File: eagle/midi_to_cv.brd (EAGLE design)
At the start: 100.3 x 80 mm, 26 parts, among them U1 ATMEGA328P_PDIP

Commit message: noise and accent and raw gates
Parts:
- added C10: 47n, rcl:C025-040X050
- added C11: 2n7, rcl:C025-040X050
- added C12: 2n2, rcl:C025-040X050
- added C13: 1u/50v, rcl:B45181A
- added C8: 470pF, rcl:C025-040X050
- added C9: 18p, rcl:C025-040X050
- added D1, D3: (no value), SparkFun-DiscreteSemi:DIODE-1N4148
- added JP1: (no value), adafruit:2X04
- added OUTPUT: 22-23-2021, con-molex:22-23-2021
- added Q10, Q11, Q12, Q13, Q14, Q15, Q16, Q2, Q3, Q4, Q5, Q7, Q8, Q9: 2N3904, 808_lt:TO92
- added Q6: 2SK30, 808:TO92
- added R10: 1M5, rcl:0207/10
- added R11, R18, R20, R23, R25, R27, R29, R3, R31, R33, R35, R37: 15k, rcl:0207/10
- added R12: 47k, rcl:0207/10
- added R13: 100k, rcl:0207/10
- added R14: 2M2, rcl:0207/10
- added R16, R19, R21, R24, R26, R28, R30, R32, R34, R36, R38, R8, R9: 68k, rcl:0207/10
- added R17: 100k, pot:3RP/1610N
- added R7: 1M, rcl:0207/10
- added X1, X3: (no value), con-molex:22-23-2061
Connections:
- new net GND1: JP1.2, JP1.4, JP1.6, JP1.8, Q4.1, R10.2
- new net N$13: Q4.2, R10.1, R9.2
- new net N$14: Q7.1, R18.2
- new net N$15: C9.1, Q5.1, R11.2
- new net N$16: Q5.2, R12.2
- new net N$21: C9.2, D1.A, R13.1
- new net N$22: C10.1, D1.C, D3.C, R14.1
- new net N$23: D3.A, Q6.2
- new net N$24: C12.1, R16.1, R17.2, X1.1, X1.2, X1.3, X1.4, X1.5, X1.6, X3.1, X3.2, X3.3, X3.4, X3.5, X3.6
- new net N$25: Q7.2, R19.2
- new net N$26: C13.-, OUTPUT.2
- new net N$27: Q8.1, R20.2
- new net N$28: Q8.2, R21.2
- new net N$29: C11.1, C12.2, Q6.1, R17.3
- new net N$3: Q2.1, R3.2
- new net N$30: Q9.1, R23.2
- new net N$31: Q9.2, R24.2
- new net N$32: C11.2, C13.+, Q6.3, R16.2
- new net N$33: Q10.1, R25.2
- new net N$34: Q10.2, R26.2
- new net N$35: R21.1, U1.23
- new net N$36: Q11.1, R27.2
- new net N$37: Q11.2, R28.2
- new net N$38: Q12.1, R29.2
- new net N$39: Q12.2, R30.2
- new net N$40: Q13.1, R31.2
- new net N$41: Q13.2, R32.2
- new net N$42: Q14.1, R33.2
- new net N$43: Q14.2, R34.2
- new net N$44: Q15.1, R35.2
- new net N$45: Q15.2, R36.2
- new net N$46: Q16.1, R37.2
- new net N$47: Q16.2, R38.2
- new net N$48: R30.1, U1.24
- new net N$49: R36.1, U1.25
- new net N$50: R8.1, U1.26
- new net N$51: R19.1, U1.28
- new net N$52: R28.1, U1.27
- new net N$53: R34.1, U1.4
- new net N$54: R26.1, U1.5
- new net N$55: R24.1, U1.6
- new net N$56: R32.1, U1.11
- new net N$57: R38.1, U1.12
- new net N$6: C8.1, Q3.3, R7.2
- new net N$7: Q2.2, R8.2
- new net N$8: C8.2, R9.1
- net +12V: now also R11.1, R18.1, R20.1, R23.1, R25.1, R27.1, R29.1, R3.1, R31.1, R33.1, R35.1, R37.1, R7.1
- net GND: now also C10.2, JP1.1, JP1.3, JP1.5, JP1.7, OUTPUT.1, Q10.3, Q11.3, Q12.3, Q13.3, Q14.3, Q15.3, Q16.3, Q2.3, Q3.2, Q4.3, Q5.3, Q7.3, Q8.3, Q9.3, R13.2

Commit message: connectors for each voice
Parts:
- removed JP1: (no value), adafruit:2X04
- removed LED: 22-23-2021, con-molex:22-23-2021
- removed MIDI_OUT_THRU1: 22-23-2031, con-molex:22-23-2031
- removed Q10, Q11, Q12, Q13, Q14, Q15, Q16, Q2, Q7, Q8, Q9: 2N3904, 808_lt:TO92
- removed R18, R20, R23, R25, R27, R29, R3, R31, R33, R35, R37: 15k, rcl:0207/10
- removed R19, R21, R24, R26, R28, R30, R32, R34, R36, R38, R8: 68k, rcl:0207/10
- removed R2: 220, rcl:0207/10
- removed R4: 4.7k, rcl:0207/10
- removed X1, X3: (no value), con-molex:22-23-2061
- added BD, HB, LB, LC: 22-23-2041, con-molex:22-23-2041
- added CB, C_RS, MB, SD: 22-23-2051, con-molex:22-23-2051
- added CY, GU, HH, M: (no value), con-molex:22-23-2061
- added TB: 22-23-2071, con-molex:22-23-2071
- R1, R10, R11, R13, R14, R16, R22, R6, R7, R9: device rcl:0207/10 -> rcl:0204/7
- R12: device rcl:0207/10 -> rcl:0207/12
- moved C13 180.3 mm to (21.6, 20.3), turned to 270 degrees
- moved OUTPUT 169.2 mm to (24.1, 10.2), turned to 180 degrees
- moved R16 151.8 mm to (20.3, 10.2), turned to 90 degrees
- moved C12 146.3 mm to (11.4, 12.7)
- moved C11 142.9 mm to (16.5, 17.8)
- moved R17 133.6 mm to (10.2, 3.81)
- moved Q6 125.4 mm to (17.8, 24.1), turned to 90 degrees
- moved C8 113.7 mm to (74.9, 53.3)
- moved D3 113.1 mm to (8.89, 17.8), turned to 180 degrees
- moved R14 111.8 mm to (2.54, 20.3), turned to 90 degrees
- moved C10 111.8 mm to (3.81, 27.9), turned to 180 degrees
- moved R10 109.2 mm to (66.0, 44.5), turned to 270 degrees
- moved Q4 107.1 mm to (62.2, 47.0), turned to 270 degrees
- moved R13 106.7 mm to (6.35, 31.8), turned to 180 degrees
- moved R12 105.6 mm to (24.1, 41.9), turned to 270 degrees
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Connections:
- removed net GND1: JP1.2, JP1.4, JP1.6, JP1.8, Q4.1, R10.2
- removed net N$10: R4.2, U1.19
- removed net N$11: LED.2, R4.1
- removed net N$12: MIDI_OUT_THRU1.2, U1.3
- removed net N$27: Q8.1, R20.2
- removed net N$28: Q8.2, R21.2
- removed net N$30: Q9.1, R23.2
- removed net N$31: Q9.2, R24.2
- removed net N$33: Q10.1, R25.2
- removed net N$34: Q10.2, R26.2
- removed net N$35: R21.1, U1.23
- removed net N$36: Q11.1, R27.2
- removed net N$37: Q11.2, R28.2
- removed net N$38: Q12.1, R29.2
- removed net N$39: Q12.2, R30.2
- removed net N$40: Q13.1, R31.2
- removed net N$41: Q13.2, R32.2
- removed net N$42: Q14.1, R33.2
- removed net N$43: Q14.2, R34.2
- removed net N$44: Q15.1, R35.2
- removed net N$45: Q15.2, R36.2
- removed net N$46: Q16.1, R37.2
- removed net N$47: Q16.2, R38.2
- removed net N$48: R30.1, U1.24
- removed net N$49: R36.1, U1.25
- removed net N$50: R8.1, U1.26
- removed net N$51: R19.1, U1.28
- removed net N$52: R28.1, U1.27
- removed net N$53: R34.1, U1.4
- removed net N$54: R26.1, U1.5
- removed net N$55: R24.1, U1.6
- removed net N$56: R32.1, U1.11
- removed net N$57: R38.1, U1.12
- removed net N$9: MIDI_OUT_THRU1.1, R2.2
- new net ACCENT: R12.1, U1.5
- new net CB_TRIG: CB.1, U1.28
- new net CY_KILL: CY.2, HH.2, M.2, U1.14
- new net CY_TRIG: CY.1, U1.16
- new net C_TRIG: C_RS.2, U1.18
- new net GU_LONG: GU.1, U1.3
- new net GU_SHORT: GU.2, U1.4
- new net HH_TRIG: HH.1, U1.15
- new net M_TRIG: M.1, U1.13
- new net NOISE: CY.3, GU.3, HH.3, M.3, Q4.1, R10.2, SD.2, TB.4
- new net RETURN: BD.4, C12.1, CB.5, CY.6, C_RS.5, GU.6, HB.4, HH.6, LB.4, LC.4, M.6, MB.5, R16.1, R17.2, SD.5, TB.7
- new net RS_TRIG: C_RS.1, U1.17
- new net SD_TRIG: SD.1, U1.19
- new net TB_KILL: TB.3, U1.12
- new net TB_LONG: TB.1, U1.6
- new net TB_SHORT: TB.2, U1.11
- net +12V: now also BD.2, CB.3, CY.4, C_RS.3, GU.4, HB.2, HH.4, LB.2, LC.2, M.4, MB.3, SD.3, TB.5; no longer R18.1, R20.1, R23.1, R25.1, R27.1, R29.1, R3.1, R31.1, R33.1, R35.1, R37.1
- net +5V: now also CB.2, MB.2; no longer R2.1
- net GND: now also BD.3, CB.4, CY.5, C_RS.4, GU.5, HB.3, HH.5, LB.3, LC.3, M.5, MB.4, R14.2, SD.4, TB.6; no longer JP1.1, JP1.3, JP1.5, JP1.7, LED.1, MIDI_OUT_THRU1.3, Q10.3, Q11.3, Q12.3, Q13.3, Q14.3, Q15.3, Q16.3, Q2.3, Q7.3, Q8.3, Q9.3
- net N$14: now also HB.1, U1.25; no longer Q7.1, R18.2
- net N$24: now also MB.1, U1.27; no longer C12.1, R16.1, R17.2, X1.1, X1.2, X1.3, X1.4, X1.5, X1.6, X3.1, X3.2, X3.3, X3.4, X3.5, X3.6
- net N$25: now also LC.1, U1.26; no longer Q7.2, R19.2
- net N$3: now also BD.1, U1.23; no longer Q2.1, R3.2
- net N$7: now also LB.1, U1.24; no longer Q2.2, R8.2
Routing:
- net +5V: track 230.1 -> 0.00 mm, vias 6 -> 0
- net GND: track 177.2 -> 0.00 mm
- net +12V: track 158.0 -> 0.00 mm, vias 2 -> 0
- net N$17: track 22.8 -> 0.00 mm
- net N$62: track 17.8 -> 0.00 mm
- net N$20: track 17.7 -> 0.00 mm
- net N$12: track 16.9 -> 0.00 mm
- net N$2: track 16.8 -> 0.00 mm
- net N$10: track 16.7 -> 0.00 mm
- net N$5: track 15.6 -> 0.00 mm
- net N$4: track 13.3 -> 0.00 mm
- net N$18: track 13.0 -> 0.00 mm
- net N$60: track 12.4 -> 0.00 mm
- net N$19: track 10.6 -> 0.00 mm
- net N$1: track 6.57 -> 0.00 mm
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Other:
- board size 100.3 x 80 mm -> 100 x 80 mm

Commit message: 95pct auto
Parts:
- C9: device rcl:C025-040X050 -> rcl:C050-025X075
- moved R14 65.1 mm to (67.3, 14.0), turned to 270 degrees
- moved Q5 65.0 mm to (80.0, 29.2), turned to 90 degrees
- moved R17 63.5 mm to (73.7, 3.81)
- moved C10 62.5 mm to (64.8, 14.0), turned to 270 degrees
- moved C9 62.3 mm to (73.7, 30.5)
- moved D3 62.3 mm to (71.1, 20.3)
- moved C12 62.2 mm to (73.7, 11.4)
- moved R13 61.3 mm to (67.3, 25.4)
- moved R11 60.3 mm to (78.7, 38.1), turned to 270 degrees
- moved C13 59.8 mm to (81.3, 24.1)
- moved D1 59.7 mm to (67.3, 22.9), turned to 180 degrees
- moved Q6 59.7 mm to (77.5, 24.1)
- moved C11 57.2 mm to (73.7, 15.2), turned to 180 degrees
- moved OUTPUT 54.7 mm to (78.7, 14.0)
- moved R16 49.6 mm to (69.8, 12.7)
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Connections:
- removed net GU_LONG: GU.1, U1.3
- removed net GU_SHORT: GU.2, U1.4
- new net N$10: GU.2, U1.19
- new net N$9: GU.1, U1.18
- net ACCENT: now also U1.28; no longer U1.5
- net CB_TRIG: now also U1.5; no longer U1.28
- net CY_KILL: now also U1.13; no longer U1.14
- net C_TRIG: now also U1.24; no longer U1.18
- net M_TRIG: now also U1.14; no longer U1.13
- net N$3: now also U1.3; no longer U1.23
- net N$7: now also U1.4; no longer U1.24
- net RS_TRIG: now also U1.23; no longer U1.17
- net SD_TRIG: now also U1.17; no longer U1.19
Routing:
- net GND: track 0.00 -> 442.4 mm
- net RETURN: track 0.00 -> 227.4 mm
- net +12V: track 0.00 -> 174.4 mm
- net +5V: track 0.00 -> 80.8 mm
- net NOISE: track 0.00 -> 72.5 mm
- net CY_KILL: track 0.00 -> 47.1 mm
- net N$5: track 0.00 -> 29.7 mm
- net HH_TRIG: track 0.00 -> 22.8 mm
- net TB_KILL: track 0.00 -> 22.5 mm
- net N$17: track 0.00 -> 22.5 mm
- net N$29: track 0.00 -> 21.8 mm
- net TB_SHORT: track 0.00 -> 20.9 mm
- net N$32: track 0.00 -> 20.5 mm
- net N$7: track 0.00 -> 20.3 mm
- net N$4: track 0.00 -> 19.5 mm
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
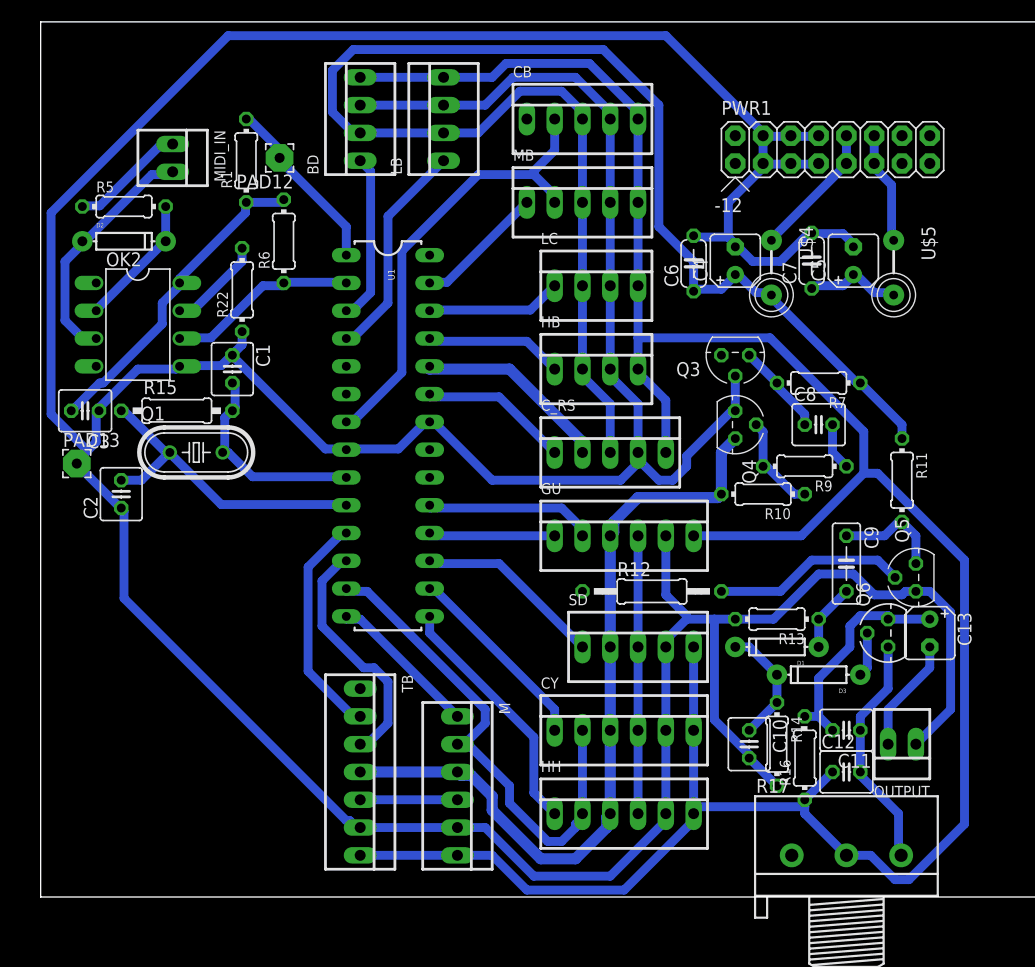
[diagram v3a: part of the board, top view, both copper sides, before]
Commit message: added midi led and thru
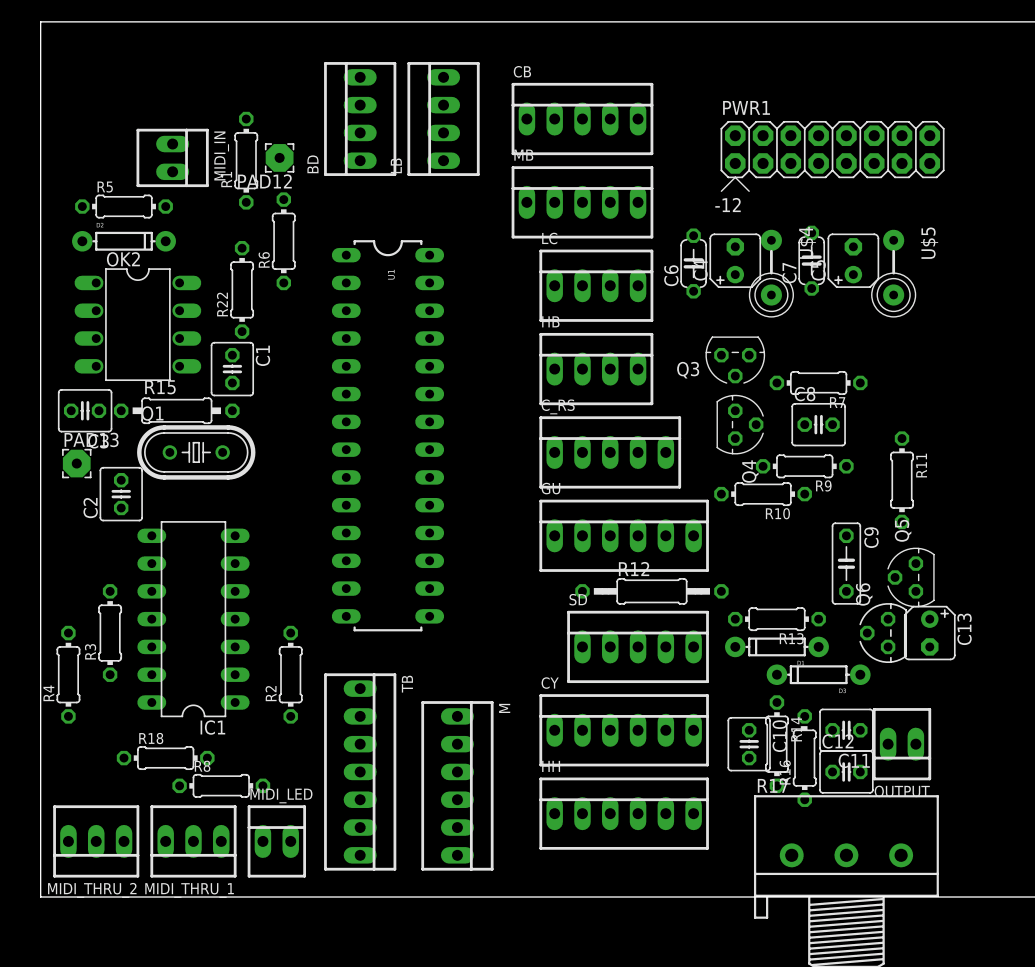
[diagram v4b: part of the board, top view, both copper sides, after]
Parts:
- added IC1: 4093N, 40xx:DIL14
- added MIDI_LED: 22-23-2021, con-molex:22-23-2021
- added MIDI_THRU_1, MIDI_THRU_2: 22-23-2031, con-molex:22-23-2031
- added R18, R3, R4, R8: 220, rcl:0204/7
- added R2: 330, rcl:0204/7
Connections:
- new net N$11: IC1.1, IC1.2, OK2.6, R6.1, U1.2
- new net N$12: IC1.4, R2.2
- new net N$27: IC1.10, R3.2
- new net N$28: IC1.11, R4.2
- new net N$30: IC1.12, IC1.13, IC1.3, IC1.5, IC1.6, IC1.8, IC1.9
- new net N$31: MIDI_LED.2, R2.1
- new net N$33: MIDI_THRU_1.3, R3.1
- new net N$34: MIDI_THRU_2.3, R4.1
- new net N$35: MIDI_THRU_2.1, R18.1
- net +5V: now also IC1.14, MIDI_LED.1, R18.2, R8.2
- net GND: now also IC1.7, MIDI_THRU_1.2, MIDI_THRU_2.2
- net N$20: now also MIDI_THRU_1.1, R8.1; no longer OK2.6, R6.1, U1.2
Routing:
- net GND: track 442.4 -> 0.00 mm
- net RETURN: track 227.4 -> 0.00 mm
- net +12V: track 174.4 -> 0.00 mm
- net +5V: track 80.8 -> 0.00 mm
- net NOISE: track 72.5 -> 0.00 mm
- net CY_KILL: track 47.1 -> 0.00 mm
- net N$5: track 29.7 -> 0.00 mm
- net HH_TRIG: track 22.8 -> 0.00 mm
- net TB_KILL: track 22.5 -> 0.00 mm
- net N$17: track 22.5 -> 0.00 mm
- net N$29: track 21.8 -> 0.00 mm
- net TB_SHORT: track 20.9 -> 0.00 mm
- net N$32: track 20.5 -> 0.00 mm
- net N$7: track 20.3 -> 0.00 mm
- net N$4: track 19.5 -> 0.00 mm
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
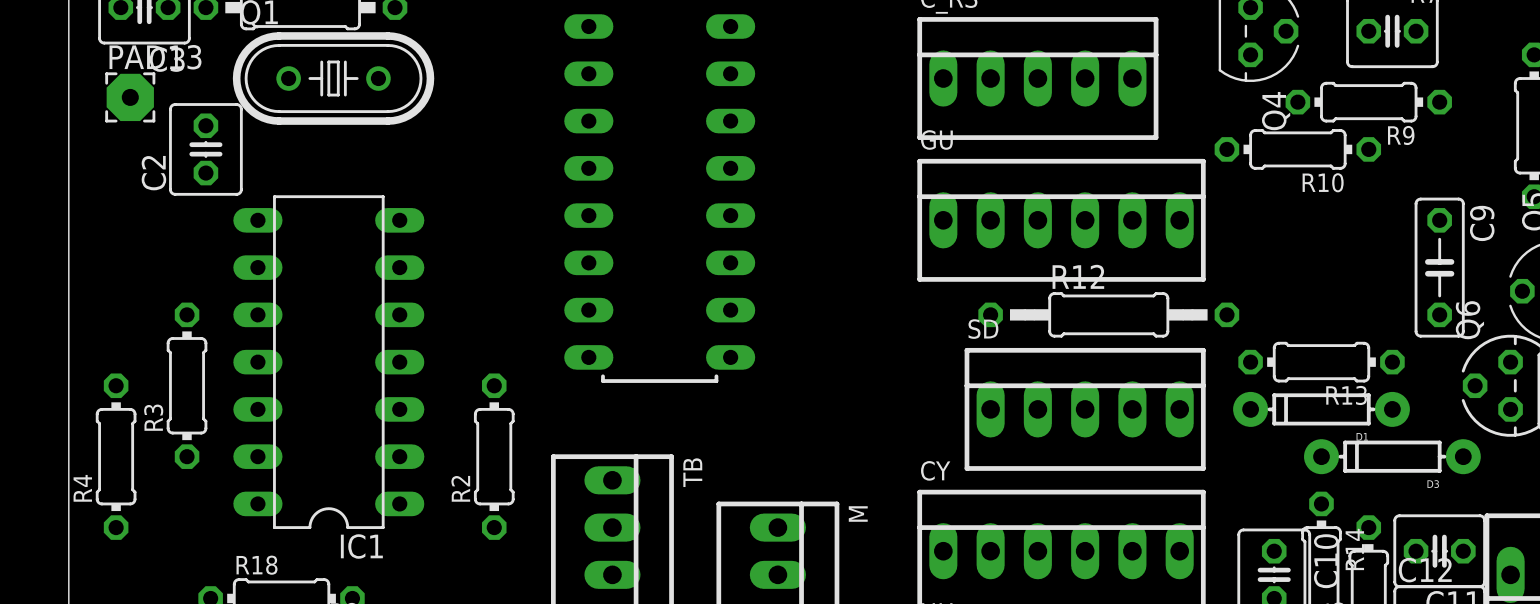
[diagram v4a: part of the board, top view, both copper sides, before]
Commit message: shifted accent pin closer to circuit
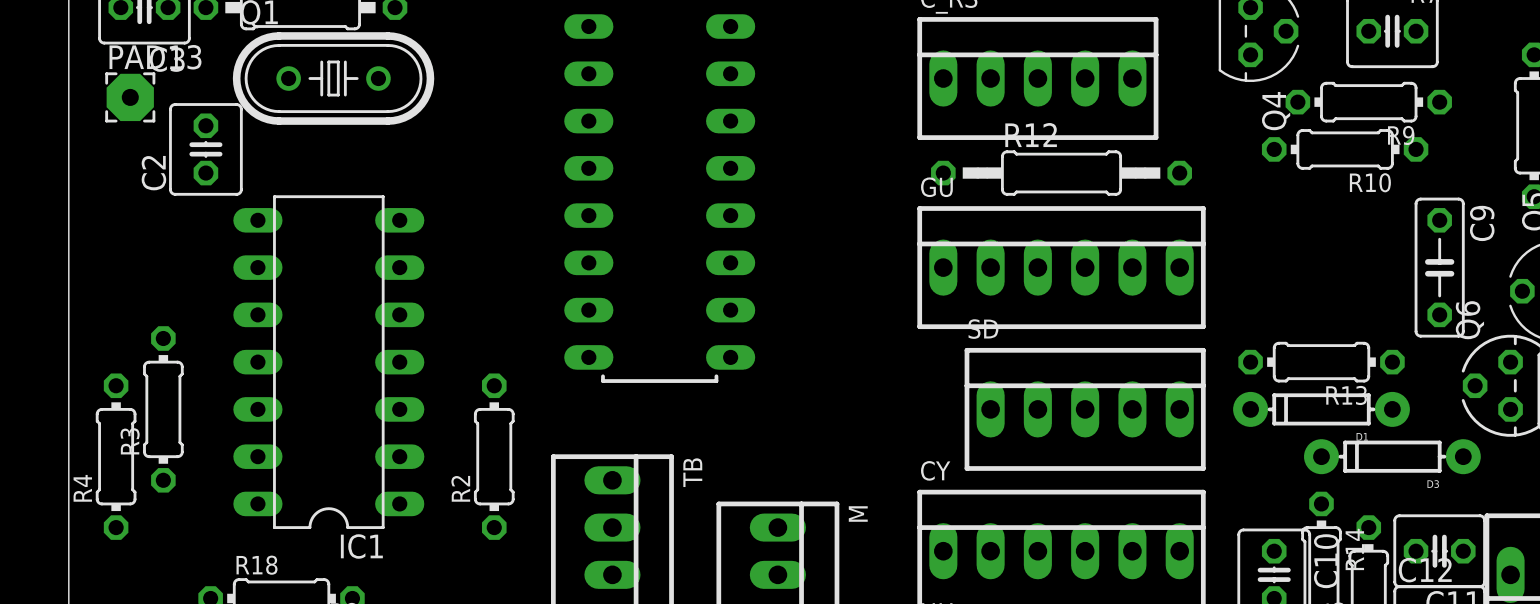
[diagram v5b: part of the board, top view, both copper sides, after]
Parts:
- moved R12 8.03 mm to (53.3, 35.6)
- moved GU 2.54 mm to (53.3, 30.5)
- moved R10 2.54 mm to (68.6, 36.8)
- moved R3 1.80 mm to (5.08, 22.9)
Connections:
- net ACCENT: now also U1.23; no longer U1.28
- net C_TRIG: now also U1.25; no longer U1.24
- net N$11: now also IC1.5, IC1.6; no longer IC1.1, IC1.2
- net N$12: now also IC1.3; no longer IC1.4
- net N$14: now also U1.26; no longer U1.25
- net N$24: now also U1.28; no longer U1.27
- net N$25: now also U1.27; no longer U1.26
- net N$30: now also IC1.1, IC1.2, IC1.4; no longer IC1.3, IC1.5, IC1.6
- net RS_TRIG: now also U1.24; no longer U1.23

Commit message: tweaks toward auto
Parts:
- R15: device rcl:0207/10 -> rcl:0204/7
- moved C2 17.2 mm to (22.9, 29.5), turned to 0 degrees
- moved C3 12.5 mm to (16.5, 45.5), turned to 90 degrees
- moved PAD13 10.9 mm to (13.5, 43.4)
- moved Q1 9.34 mm to (22.9, 37.1), turned to 90 degrees
- moved R15 8.49 mm to (19.1, 39.1), turned to 90 degrees
- moved C1 6.41 mm to (22.9, 44.7), turned to 180 degrees
- moved R2 2.84 mm to (20.3, 19.1)
- moved IC1 2.54 mm to (14.0, 22.9)
- moved BD 2.54 mm to (29.2, 73.7)
- moved LB 2.54 mm to (36.8, 73.7)
- moved R4 1.80 mm to (3.81, 19.1)
- moved R3 1.80 mm to (6.35, 21.6)

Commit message: 96pct auto
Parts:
- R1: device rcl:0204/7 -> rcl:0204/5
- R12: device rcl:0207/12 -> rcl:0207/15
- moved PAD13 30.7 mm to (26.2, 71.4)
- moved C3 26.4 mm to (21.3, 71.4), turned to 270 degrees
- moved C6 25.9 mm to (85.6, 58.4), turned to 180 degrees
- moved C4 22.2 mm to (85.3, 62.2), turned to 180 degrees
- moved U$4 20.2 mm to (84.7, 66.8), turned to 0 degrees
- moved C2 14.5 mm to (26.7, 43.4), turned to 180 degrees
- moved PWR1 12.7 mm to (81.3, 73.9), turned to 180 degrees
- moved MB 12.0 mm to (61.0, 67.3)
- moved R9 10.2 mm to (80.0, 40.6)
- moved C11 10.2 mm to (83.8, 16.5)
- moved C12 10.2 mm to (83.8, 12.7)
- moved OUTPUT 10.2 mm to (88.9, 14.0)
- moved U$5 10.1 mm to (74.0, 66.8), turned to 180 degrees
- moved R15 10.0 mm to (29.0, 40.6), turned to 0 degrees
- moved R11 9.67 mm to (87.6, 41.9)
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
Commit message: 97pct auto
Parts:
- moved C6 15.8 mm to (69.8, 59.2), turned to 90 degrees
- moved C4 12.0 mm to (73.7, 59.4), turned to 90 degrees
- moved C7 11.8 mm to (70.5, 70.1), turned to 270 degrees
- moved PWR1 11.7 mm to (86.6, 63.5), turned to 90 degrees
- moved U$4 9.34 mm to (78.2, 60.1), turned to 270 degrees
- moved PAD12 8.13 mm to (32.5, 62.5)
- moved C5 7.25 mm to (74.3, 70.1), turned to 270 degrees
- moved U$5 5.75 mm to (78.2, 70.7), turned to 90 degrees
- moved CB 2.54 mm to (48.3, 69.8)
- moved LC 1.27 mm to (58.4, 59.7)
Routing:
- net GND: track 0.00 -> 445.5 mm
- net RETURN: track 0.00 -> 280.2 mm
- net +12V: track 0.00 -> 157.2 mm
- net +5V: track 0.00 -> 136.2 mm
- net NOISE: track 0.00 -> 76.0 mm
- net TB_LONG: track 0.00 -> 45.4 mm
- net CY_KILL: track 0.00 -> 45.0 mm
- net N$11: track 0.00 -> 37.5 mm
- net N$30: track 0.00 -> 30.0 mm
- net N$16: track 0.00 -> 24.0 mm
- net TB_SHORT: track 0.00 -> 23.9 mm
- net TB_KILL: track 0.00 -> 23.7 mm
- net N$29: track 0.00 -> 23.2 mm
- net CB_TRIG: track 0.00 -> 22.4 mm
- net HH_TRIG: track 0.00 -> 21.5 mm
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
